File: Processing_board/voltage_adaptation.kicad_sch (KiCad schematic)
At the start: 20 parts, among them J19 Conn_01x03_Pin, J20 Conn_01x03_Pin, Q5 DMP3056LSS-13, U12 LD1117S50TR_SOT223, U17 LD1117S33TR_SOT223, U18 LD1117DT18TR

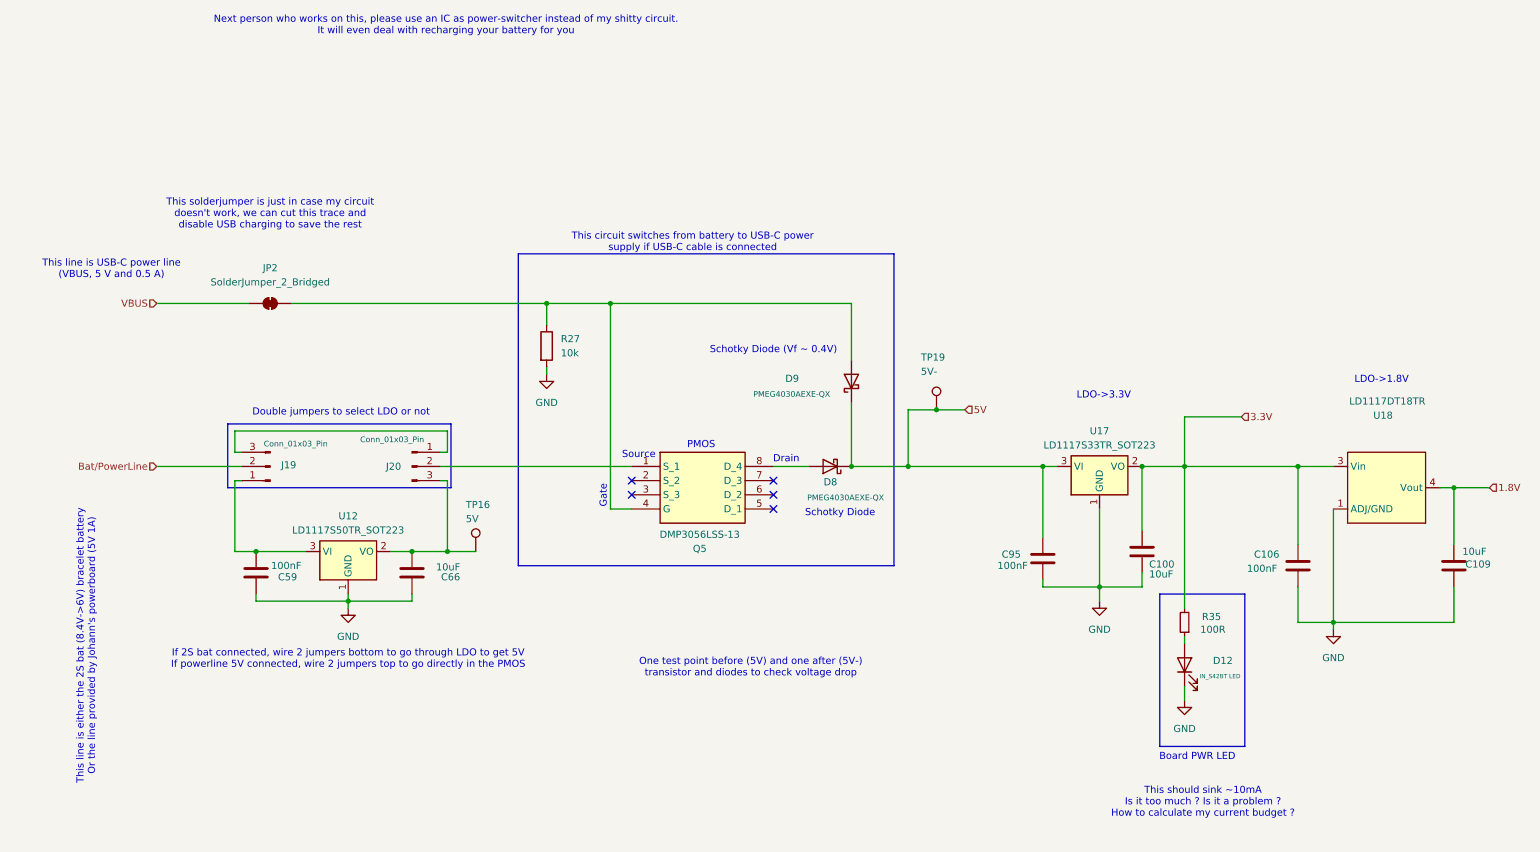
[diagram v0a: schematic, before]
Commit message: had to rename all components on the PCB to match the schematic
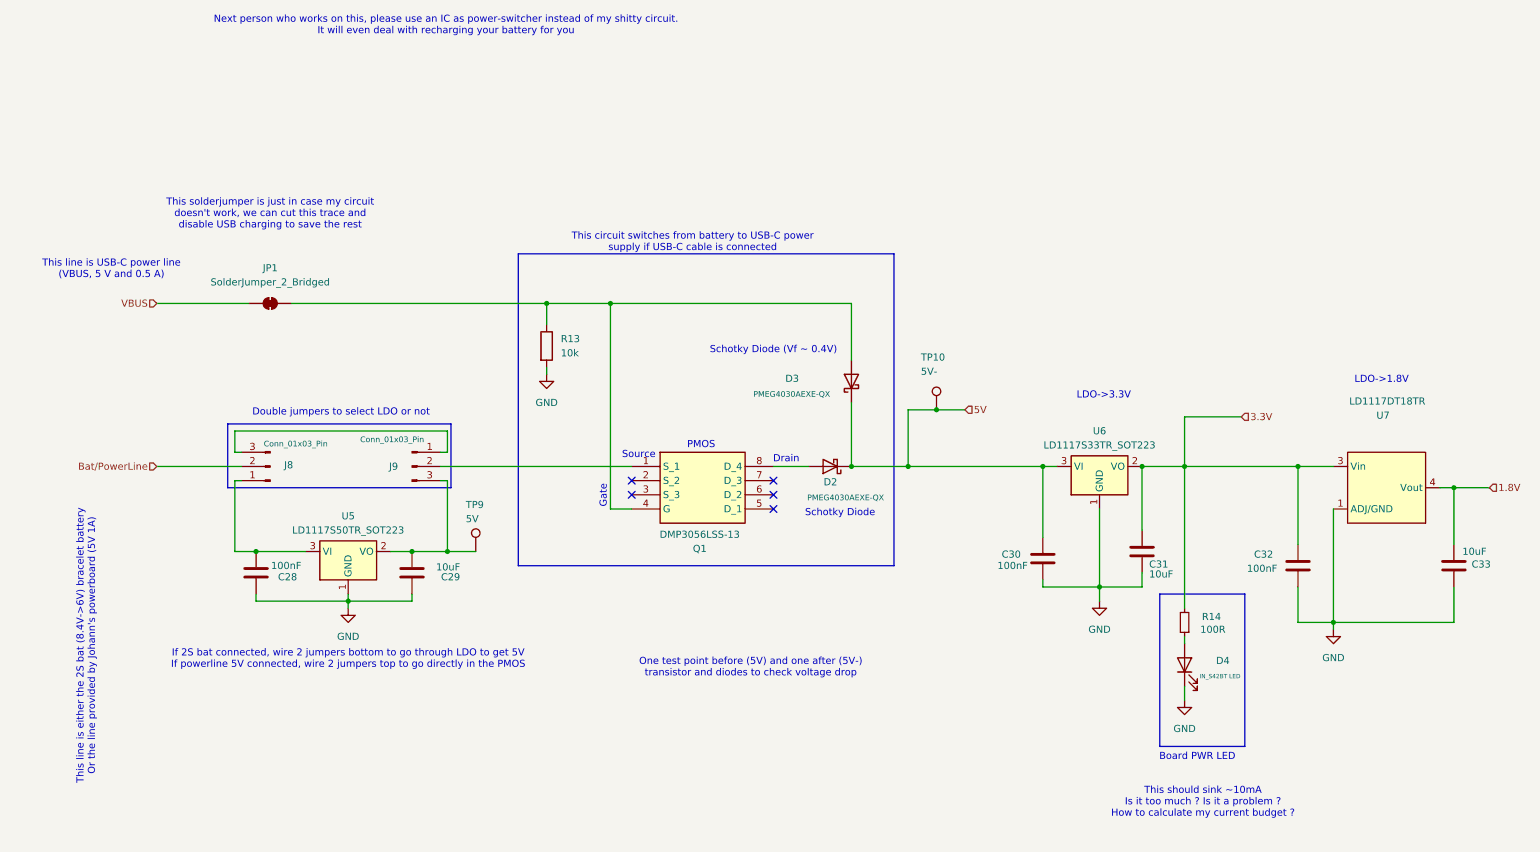
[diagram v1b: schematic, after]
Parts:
- renumbered C59 to C28, C66 to C29, C95 to C30, C100 to C31, C106 to C32, C109 to C33, D8 to D2, D9 to D3, D12 to D4, J19 to J8, J20 to J9, JP2 to JP1, Q5 to Q1, R27 to R13, R35 to R14, TP19 to TP10, TP16 to TP9, U12 to U5, U17 to U6, U18 to U7

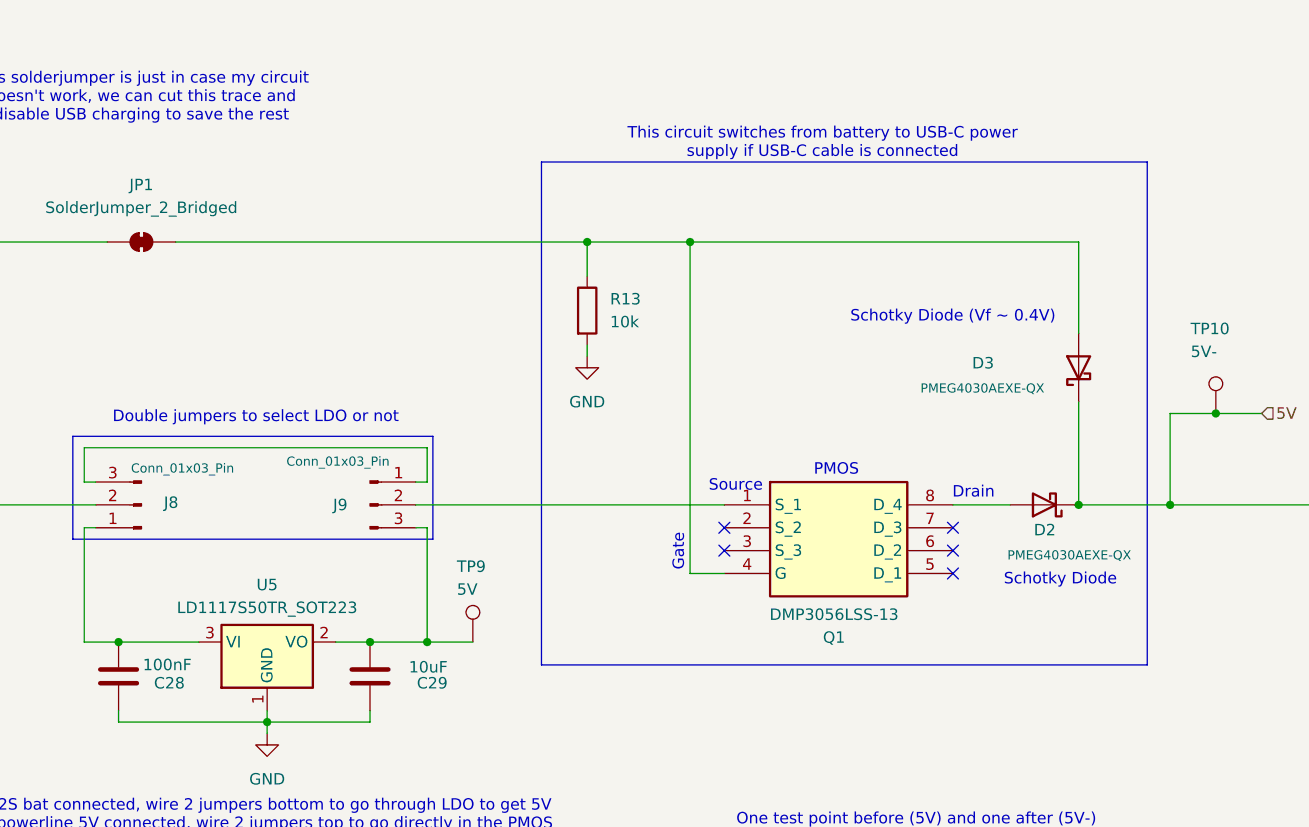
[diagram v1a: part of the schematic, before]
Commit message: created BOM, deleted useless folder Components and renamed CAD_Models to Parts
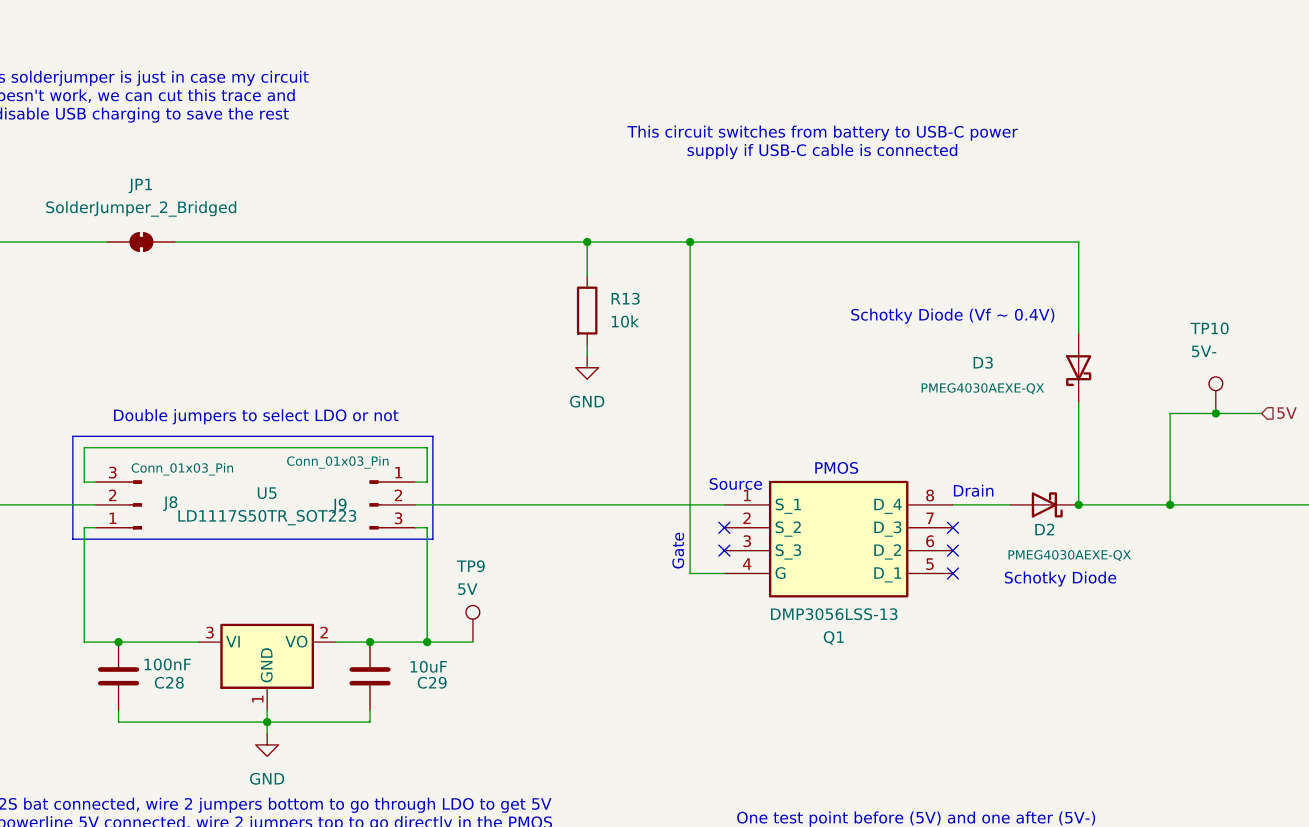
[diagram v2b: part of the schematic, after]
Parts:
- C28, C30, C32: Link (none) -> https://www.mouser.ch/ProductDetail/Samsung-Electro-Mechani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; MANUFACTURER (none) -> Samsung Electro-Mechanics; Manufacturer_Part_Number (none) -> CL05B104KP5VPNC; Panier (none) -> 1
- C29, C31, C33: Link (none) -> https://www.mouser.ch/ProductDetail/Murata-Electronics/GRM1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; MANUFACTURER (none) -> Murata Electronics; Manufacturer_Part_Number (none) -> GRM155R61A106ME11D; Panier (none) -> 1
- D2, D3: Link (none) -> https://www.mouser.ch/ProductDetail/Nexperia/PMEG4030AEXE-Q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; MANUFACTURER (none) -> Nexperia; déjà (none) -> 1
- D4: Link (none) -> https://www.mouser.ch/ProductDetail/Inolux/IN-S42BT5G?qs=mA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; MANUFACTURER (none) -> Inolux; Manufacturer_Part_Number (none) -> IN-S42BT5G; Panier (none) -> 1
- Q1: Link (none) -> https://www.mouser.ch/ProductDetail/Diodes-Incorporated/DMP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; MANUFACTURER (none) -> Diodes Incorporated; Panier (none) -> 1
- R13: Link (none) -> https://www.mouser.ch/ProductDetail/Wurth-Elektronik/560112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; MANUFACTURER (none) -> Wurth Elektronik; Manufacturer_Part_Number (none) -> 560112110020; Panier (none) -> 1
- R14: Link (none) -> https://www.mouser.ch/ProductDetail/KOA-Speer/RK73B1ETTPD10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; MANUFACTURER (none) -> KOA Speer; Manufacturer_Part_Number (none) -> RK73B1ETTPD101J; Panier (none) -> 1
- U5: Link (none) -> https://www.mouser.ch/ProductDetail/STMicroelectronics/LD11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; MANUFACTURER (none) -> STMicroelectronics; Manufacturer_Part_Number (none) -> LD1117S50TR; Panier (none) -> 1
- U6: Link (none) -> https://www.mouser.ch/ProductDetail/STMicroelectronics/LD11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; MANUFACTURER (none) -> STMicroelectronics; Manufacturer_Part_Number (none) -> LD1117S33TR; déjà (none) -> 1
- U7: Link (none) -> https://www.mouser.ch/ProductDetail/STMicroelectronics/LD11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; MANUFACTURER (none) -> STMicroelectronics; Manufacturer_Part_Number (none) -> LD1117DT18TR; déjà (none) -> 1

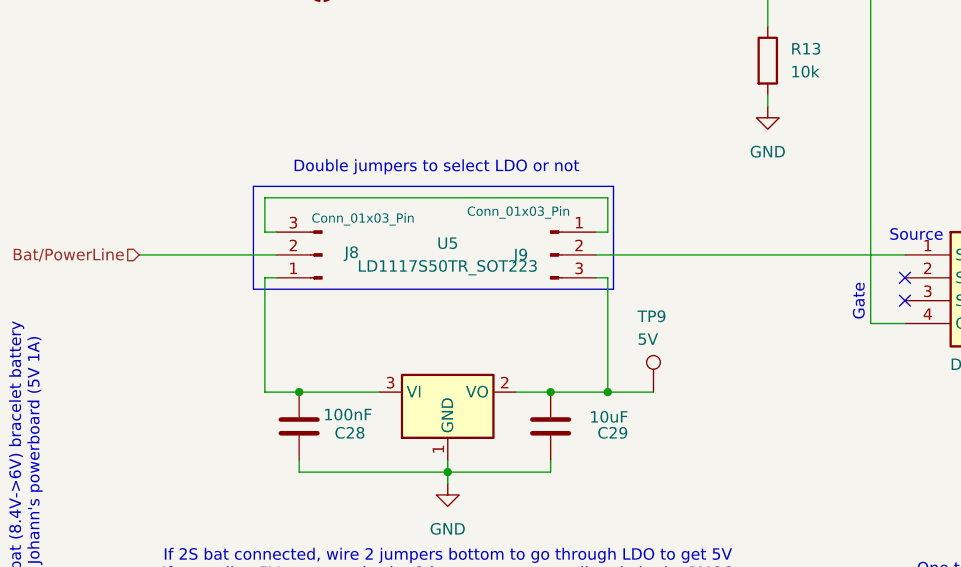
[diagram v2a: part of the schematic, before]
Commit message: correct text height/width for silkscreen, correct 3D models for THT pin headers
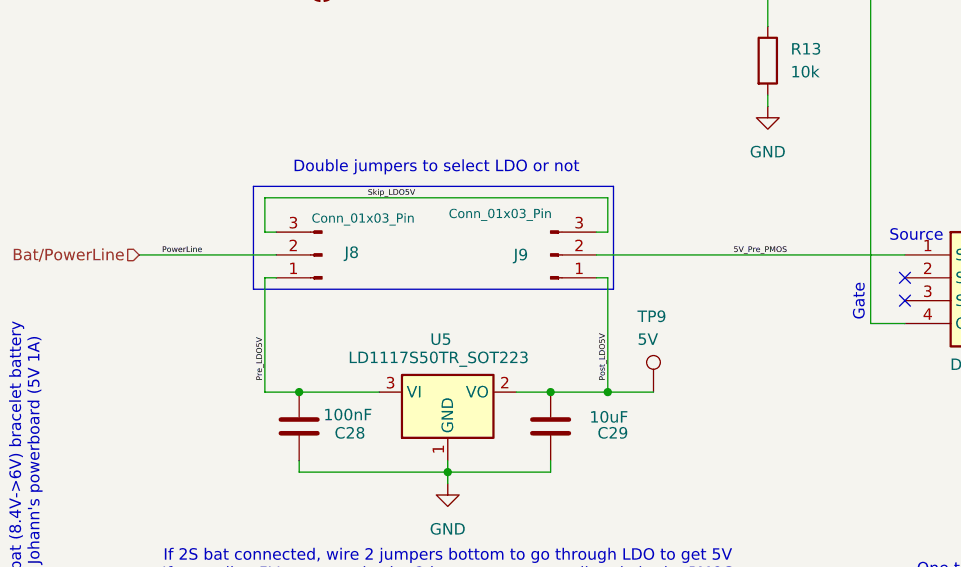
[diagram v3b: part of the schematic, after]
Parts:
- J8, J9: footprint Connector_PinHeader_2.54mm:PinHeader_1x03_P2.54mm_Vertical_SMD_Pin1Left -> Connector_PinSocket_2.54mm:PinSocket_1x03_P2.54mm_Vertical
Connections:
- net Post_LDO5V: now reaches C29.2, TP9.1, U5.2 (VO)
- net Post_LDO5V: now also J9.1 (Pin_1); no longer J9.3 (Pin_3)
- net Pre_LDO5V: now reaches C28.2, J8.1 (Pin_1), U5.3 (VI)
- net 5V_Pre_PMOS: now reaches J9.2 (Pin_2), Q1.1 (S_1)
- net Skip_LDO5V: now reaches J8.3 (Pin_3)
- net Skip_LDO5V: now also J9.3 (Pin_3); no longer J9.1 (Pin_1)
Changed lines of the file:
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@@
+		)
+	)
+	(label "5V_Pre_PMOS"
+		(at 101.6 101.6 0)
+		(effects
+			(font
+				(size 0.635 0.635)
+			)
+			(justify left bottom)
+		)
+	)
+	(label "Skip_LDO5V"
+		(at 60.96 95.25 0)
+		(effects
+			(font
+				(size 0.635 0.635)
+			)
+			(justify left bottom)
+		)
+	)
+	(label "Pre_LDO5V"
+		(at 49.53 115.57 90)
+		(effects
+			(font
+				(size 0.635 0.635)
+			)
+			(justify left bottom)
+		)
+	)
+	(label "PowerLine"
+		(at 38.1 101.6 0)
+		(effects
+			(font
+				(size 0.635 0.635)
+			)
+			(justify left bottom)
+		)
+	)
+	(label "Post_LDO5V"
+		(at 87.63 115.57 90)
+		(effects
+			(font
+				(size 0.635 0.635)
+			)
+			(justify left bottom)
 		)
 	)
@@
 		(lib_id "Connector:Conn_01x03_Pin")
 		(at 81.28 101.6 0)
+		(mirror x)
 		(unit 1)
 		(exclude_from_sim no)
@@
 		)
 		(property "Value" "Conn_01x03_Pin"
-			(at 77.724 96.774 0)
+			(at 75.692 97.028 0)
 			(effects
 				(font
@@
 			)
 		)
-		(property "Footprint" "Connector_PinHeader_2.54mm:PinHeader_1x03_P2.54mm_Vertical_SMD_Pin1Left"
+		(property "Footprint" "Connector_PinSocket_2.54mm:PinSocket_1x03_P2.54mm_Vertical"
 			(at 81.28 101.6 0)
 			(effects
@@
 		(on_board yes)
 		(dnp no)
-		(fields_autoplaced yes)
 		(property "Reference" "U5"
-			(at 69.85 100.33 0)
+			(at 69.088 110.998 0)
 			(effects
 				(font
@@
 		)
 		(property "Value" "LD1117S50TR_SOT223"
-			(at 69.85 102.87 0)
+			(at 68.834 113.03 0)
 			(effects
 				(font
@@
 			)
 		)
-		(property "Footprint" "Connector_PinHeader_2.54mm:PinHeader_1x03_P2.54mm_Vertical_SMD_Pin1Left"
+		(property "Footprint" "Connector_PinSocket_2.54mm:PinSocket_1x03_P2.54mm_Vertical"
 			(at 55.88 101.6 0)
 			(effects
